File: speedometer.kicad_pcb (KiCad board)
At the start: 2 copper layers, 100 x 100 mm, 47 parts, among them J1 Conn_01x03, J2 Conn_01x03, J3 Conn_01x03, J4 Conn_01x03, Q1 SSM3J332R, Q2 MMBT3904, Q3 MMBT3904, Q4 MMBT3904, Q5 L-51ROPT1D1, Q6 TMBT3906, Q7 TMBT3906, Q8 L-51ROPT1D1, Q9 TMBT3906, SW1 SW_Push, SW2 RESET_SW, U1 RaspberryPi-Pico, U2 OSL30561-IRA

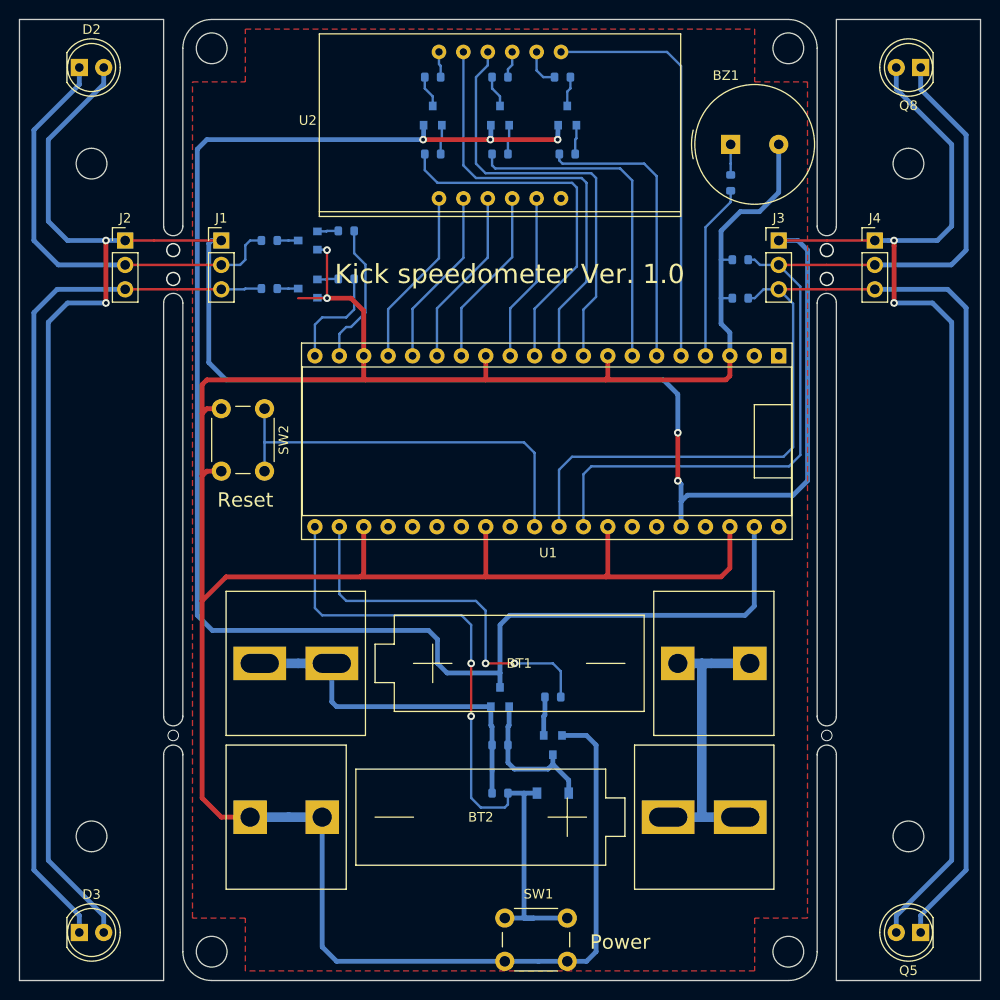
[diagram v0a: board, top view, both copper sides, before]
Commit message: v1.0での手修正部分を反映
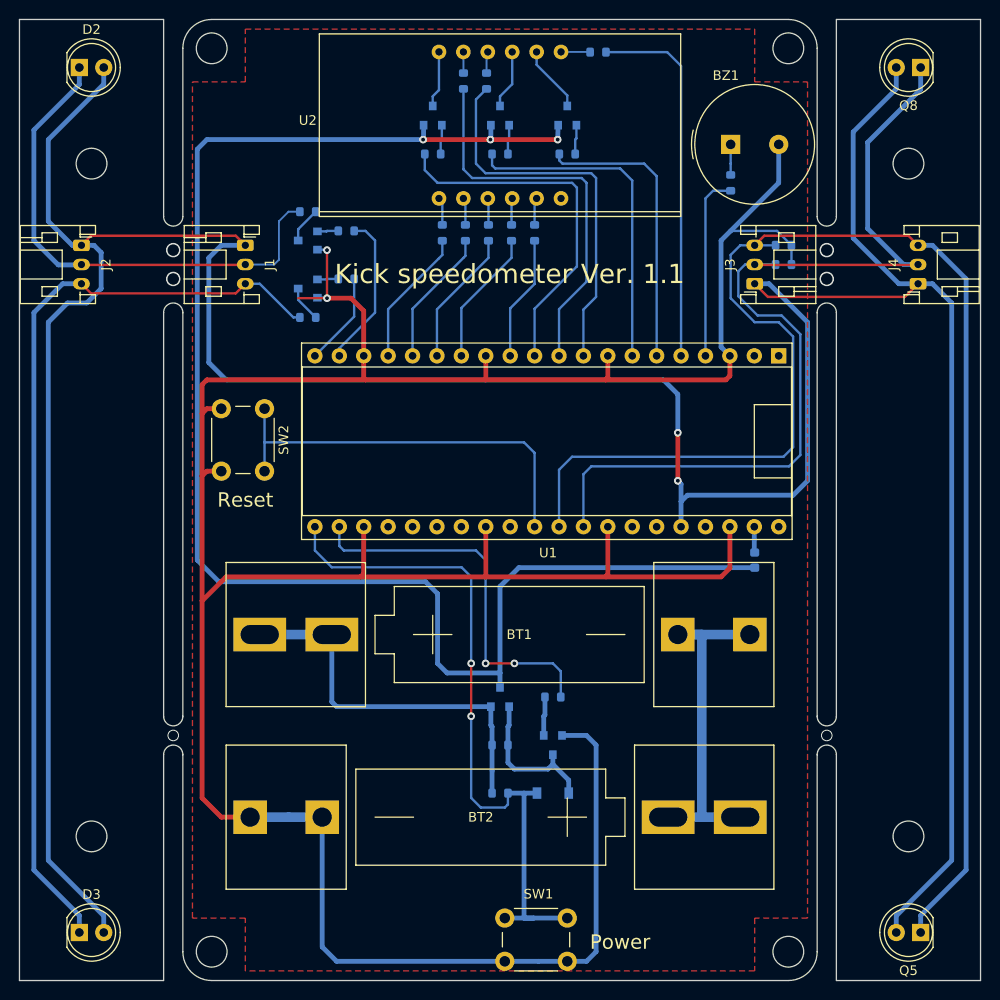
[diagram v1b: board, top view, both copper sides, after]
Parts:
- added D4: D_Small, Diode_SMD:D_0603_1608Metric, B.Cu at (76.5, 56.2)
- added R17: 200R, Resistor_SMD:R_0603_1608Metric, B.Cu at (46.4, 22.2)
- added R18: 200R, Resistor_SMD:R_0603_1608Metric, B.Cu at (44.0, 22.2)
- added R19: 200R, Resistor_SMD:R_0603_1608Metric, B.Cu at (48.6, 6.40)
- added R20: 200R, Resistor_SMD:R_0603_1608Metric, B.Cu at (53.6, 22.2)
- added R21: 200R, Resistor_SMD:R_0603_1608Metric, B.Cu at (48.8, 22.2)
- J1, J2, J3, J4: footprint Connector_PinHeader_2.54mm:PinHeader_1x03_P2.54mm_Vertical -> Connector_JST:JST_PH_S3B-PH-K_1x03_P2.00mm_Horizontal
- R14, R15, R16: value 470R -> 200R
- moved R16 17.0 mm to (51.2, 22.2), turned to 90 degrees
- moved R15 10.5 mm to (60.2, 3.40), turned to 180 degrees
- moved R12 7.11 mm to (79.5, 23.5), turned to 0 degrees
- moved J4 6.36 mm to (93.5, 27.5), turned to 90 degrees
- moved J3 5.15 mm to (76.5, 27.5), turned to 90 degrees
- moved R7 5.00 mm to (30.0, 20.0)
- moved R8 5.00 mm to (30.0, 31.0)
- moved J2 4.58 mm to (6.45, 23.5), turned to -90 degrees
- moved R13 4.53 mm to (79.5, 25.5), turned to 0 degrees
- moved R14 3.22 mm to (46.2, 6.40), turned to 90 degrees
- moved BT1 3.00 mm to (51.0, 64.0)
- moved J1 2.55 mm to (23.5, 23.5), turned to -90 degrees
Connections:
- Q6 pad 3: Net-(Q6-Pad3) -> Net-(Q6-C)
- Q7 pad 3: Net-(Q7-Pad3) -> Net-(Q7-C)
- Q9 pad 3: Net-(Q9-Pad3) -> Net-(Q9-C)
- R14 pad 1: Net-(Q6-Pad3) -> /DISP_a
- R14 pad 2: Net-(R14-Pad2) -> Net-(U2-a)
- R15 pad 1: Net-(Q7-Pad3) -> /DISP_b
- R15 pad 2: Net-(R15-Pad2) -> Net-(U2-b)
- R16 pad 1: Net-(Q9-Pad3) -> /DISP_c
- R16 pad 2: Net-(R16-Pad2) -> Net-(U2-c)
- U1 pad 1: Net-(U1-Pad1) -> unconnected-(U1-GP0-Pad1)
- U1 pad 2: Net-(U1-Pad2) -> unconnected-(U1-GP1-Pad2)
- U1 pad 24: Net-(U1-Pad24) -> unconnected-(U1-GP18-Pad24)
- U1 pad 25: Net-(U1-Pad25) -> unconnected-(U1-GP19-Pad25)
- U1 pad 26: Net-(U1-Pad26) -> unconnected-(U1-GP20-Pad26)
- U1 pad 27: Net-(U1-Pad27) -> unconnected-(U1-GP21-Pad27)
- U1 pad 29: Net-(U1-Pad29) -> unconnected-(U1-GP22-Pad29)
- U1 pad 34: Net-(U1-Pad34) -> unconnected-(U1-GP28-Pad34)
- U1 pad 35: Net-(U1-Pad35) -> unconnected-(U1-ADC_VREF-Pad35)
- U1 pad 37: Net-(U1-Pad37) -> unconnected-(U1-3V3_EN-Pad37)
- U1 pad 39: +BATT -> Net-(D4-K)
- U1 pad 40: Net-(U1-Pad40) -> unconnected-(U1-VBUS-Pad40)
- U2 pad 1: /DISP_e -> Net-(U2-e)
- U2 pad 10: /DISP_f -> Net-(U2-f)
- U2 pad 11: /DISP_a -> Net-(U2-a)
- U2 pad 12: Net-(R14-Pad2) -> Net-(Q6-C)
- U2 pad 2: /DISP_d -> Net-(U2-d)
- U2 pad 3: /DISP_dp -> Net-(U2-DPX)
- U2 pad 4: /DISP_c -> Net-(U2-c)
- U2 pad 5: /DISP_g -> Net-(U2-g)
- U2 pad 7: /DISP_b -> Net-(U2-b)
- U2 pad 8: Net-(R16-Pad2) -> Net-(Q9-C)
- U2 pad 9: Net-(R15-Pad2) -> Net-(Q7-C)
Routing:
- net /PT1: track 139.1 -> 154.7 mm
- net Net-(D2-K): track 46.6 -> 54.1 mm
- net Net-(Q9-C): track 0.00 -> 6.94 mm
- net Net-(D3-K): track 91.2 -> 97.7 mm
- net Net-(Q7-C): track 0.00 -> 6.15 mm
- net /PT0: track 94.1 -> 100.0 mm
- net Net-(Q6-C): track 0.00 -> 5.89 mm
- net GND: track 318.3 -> 323.7 mm
- net +BATT: track 168.4 -> 163.6 mm
- net /DISP_b: track 43.3 -> 38.6 mm
- net Net-(BT1--): track 32.5 -> 37.0 mm
- net /DISP_g: track 17.5 -> 13.0 mm
- net /DISP_c: track 18.6 -> 14.1 mm
- net /DISP_dp: track 18.6 -> 14.2 mm
- net /DISP_d: track 18.6 -> 14.3 mm
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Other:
- outline, holes or cut-outs redrawn
- net class Default removed
- board text added: "Kick speedometer Ver. 1.1"
- board text removed: "Kick speedometer Ver. 1.0"
